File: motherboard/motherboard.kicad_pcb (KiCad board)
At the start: 2 copper layers, 85.3 x 56.5 mm, 87 parts, among them J1 power_conn, J2 serial_comm_conn, J3 Temp_connector, J5 24VDC_connector, P1 Raspberry_Pi_+_Conn, Q1 Q_NMOS_GSD, Q11 Q_NMOS_GSD, Q12 Q_NMOS_GSD, Q2 Q_NMOS_GSD, Q3 Q_NMOS_GSD, Q4 Q_NMOS_GSD, Q5 Q_NMOS_GSD, Q6 Q_NMOS_GSD, Q7 Q_NMOS_GSD, Q8 Q_NMOS_GSD, U1 LM324, U2 LM324, U4 MCP23017_ML, U5 74AUC2G04, U6 quad_and

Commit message: Do footprint assissiation
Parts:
- removed C1: C, Capacitor_SMD:C_0603_1608Metric
- removed C2, C3: 135pF, Capacitor_SMD:C_0603_1608Metric
- removed C4, C6, C8: 100nF, Capacitor_SMD:C_0603_1608Metric
- removed C5, C7, C9: 10pF, Capacitor_SMD:C_0603_1608Metric
- removed D1, D2: D, Diode_SMD:D_0603_1608Metric
- removed D10, D11, D12, D4, D5, D6, D7, D8, D9: LED, LED_SMD:LED_0603_1608Metric
- removed D3: d, Diode_SMD:D_0603_1608Metric
- removed J1: power_conn, TerminalBlock_Phoenix:TerminalBlock_Phoenix_MKDS-1,5-2-5.08_1x02_P5.08mm_Horizontal
- removed J2: serial_comm_conn, TerminalBlock_Phoenix:TerminalBlock_Phoenix_MKDS-1,5-3-5.08_1x03_P5.08mm_Horizontal
- removed J3: Temp_connector, TerminalBlock_Phoenix:TerminalBlock_Phoenix_MKDS-1,5-3-5.08_1x03_P5.08mm_Horizontal
- removed J5: 24VDC_connector, TerminalBlock_Phoenix:TerminalBlock_Phoenix_MKDS-1,5-8-5.08_1x08_P5.08mm_Horizontal
- removed P1: Raspberry_Pi_+_Conn, Connector_PinSocket_2.54mm:PinSocket_2x20_P2.54mm_Vertical
- removed Q1, Q11, Q12, Q2, Q3, Q4, Q5, Q6, Q7, Q8: Q_NMOS_GSD, Package_TO_SOT_SMD:SOT-23
- removed R1, R2: 100, Resistor_SMD:R_0603_1608Metric_Pad1.05x0.95mm_HandSolder
- removed R10, R12, R14, R16, R43, R45, R6, R8: 5, Resistor_SMD:R_0603_1608Metric_Pad1.05x0.95mm_HandSolder
- removed R11, R13, R15, R27, R28, R42, R44, R5, R7, R9: 100k, Resistor_SMD:R_0603_1608Metric_Pad1.05x0.95mm_HandSolder
- removed R17, R18, R19, R21, R32, R33, R34, R36: 4k7, Resistor_SMD:R_0603_1608Metric_Pad1.05x0.95mm_HandSolder
- removed R20, R22, R31, R35, R37, R38, R39, R40, R41: 240, Resistor_SMD:R_0603_1608Metric_Pad1.05x0.95mm_HandSolder
- removed R23, R24: 10k, Resistor_SMD:R_0603_1608Metric_Pad1.05x0.95mm_HandSolder
- removed R25, R26: 1k, Resistor_SMD:R_0603_1608Metric_Pad1.05x0.95mm_HandSolder
- removed R29: 3k3, Resistor_SMD:R_0603_1608Metric_Pad1.05x0.95mm_HandSolder
- removed R3: 4.7k, Resistor_SMD:R_0603_1608Metric_Pad1.05x0.95mm_HandSolder
- removed R30: 5k6, Resistor_SMD:R_0603_1608Metric_Pad1.05x0.95mm_HandSolder
- removed R4: 230, Resistor_SMD:R_0603_1608Metric_Pad1.05x0.95mm_HandSolder
- removed RV1: 10k, Potentiometer_SMD:Potentiometer_Vishay_TS53YL_Vertical
- removed U1, U2: LM324, Package_SO:TSSOP-14-1EP_4.4x5mm_P0.65mm
- removed U4: MCP23017_ML, Package_DFN_QFN:QFN-28-1EP_6x6mm_P0.65mm_EP4.25x4.25mm
- removed U5: 74AUC2G04, Package_TO_SOT_SMD:SOT-23-6
- removed U6: quad_and, Package_SO:SOIC-14_3.9x8.7mm_P1.27mm
- added C101: 1u, Capacitor_SMD:CP_Elec_4x5.4, F.Cu at (89.6, 43.2)
- added C102: 1u, Capacitor_SMD:CP_Elec_4x5.4, F.Cu at (74.1, 43.2)
- added C103: 1u, Capacitor_SMD:CP_Elec_4x5.4, F.Cu at (81.8, 43.2)
- added C104: 10n, Capacitor_SMD:C_0603_1608Metric_Pad1.05x0.95mm_HandSolder, F.Cu at (65.2, 94.4)
- added C105: 10n, Capacitor_SMD:C_0603_1608Metric_Pad1.05x0.95mm_HandSolder, F.Cu at (95.7, 41.5)
- added C106: 10n, Capacitor_SMD:C_0603_1608Metric_Pad1.05x0.95mm_HandSolder, F.Cu at (72.4, 47.4)
- added C107: 100p, Capacitor_SMD:C_0603_1608Metric_Pad1.05x0.95mm_HandSolder, F.Cu at (76.8, 47.4)
- added C108: 100p, Capacitor_SMD:C_0603_1608Metric_Pad1.05x0.95mm_HandSolder, F.Cu at (72.4, 49.9)
- added C109: 100p, Capacitor_SMD:C_0603_1608Metric_Pad1.05x0.95mm_HandSolder, F.Cu at (76.8, 49.9)
- added C1601: 100nF, Capacitor_SMD:C_0603_1608Metric_Pad1.05x0.95mm_HandSolder, F.Cu at (201.2, 94.5)
- added C1602: 10pF, Capacitor_SMD:C_0603_1608Metric_Pad1.05x0.95mm_HandSolder, F.Cu at (205.9, 91.1)
- added C1701: 100nF, Capacitor_SMD:C_0603_1608Metric_Pad1.05x0.95mm_HandSolder, F.Cu at (174.8, 120.1)
- added C1702: 10pF, Capacitor_SMD:C_0603_1608Metric_Pad1.05x0.95mm_HandSolder, F.Cu at (161.7, 130.3)
- added C201: 100u, Capacitor_SMD:CP_Elec_6.3x5.4_Nichicon, F.Cu at (224.7, 68.4)
- added C202: 10n, Capacitor_SMD:C_0603_1608Metric_Pad1.05x0.95mm_HandSolder, F.Cu at (212.1, 77.9)
- added C203: 68u, Capacitor_SMD:CP_Elec_6.3x5.8, F.Cu at (210.8, 72.6)
- added C204: 100n, Capacitor_SMD:C_0603_1608Metric_Pad1.05x0.95mm_HandSolder, F.Cu at (207.8, 77.9)
- added C2104: 330n, Capacitor_SMD:C_0603_1608Metric_Pad1.05x0.95mm_HandSolder, F.Cu at (142.1, 124.8)
- added C2105: 0.1u, Capacitor_SMD:C_0603_1608Metric_Pad1.05x0.95mm_HandSolder, F.Cu at (137.8, 127.3)
- added C2106: 100n, Capacitor_SMD:C_0603_1608Metric_Pad1.05x0.95mm_HandSolder, F.Cu at (137.0, 130.1)
- added C2107: 1u, Capacitor_SMD:CP_Elec_4x5.4, F.Cu at (119.6, 135.9)
- added C2201: 100n, Capacitor_SMD:C_0603_1608Metric_Pad1.05x0.95mm_HandSolder, F.Cu at (103.7, 121.9)
- added C301: 0.1u, Capacitor_SMD:C_0603_1608Metric_Pad1.05x0.95mm_HandSolder, F.Cu at (166.2, 110.8)
- added C302: 0.1u, Capacitor_SMD:C_0603_1608Metric_Pad1.05x0.95mm_HandSolder, F.Cu at (166.2, 113.3)
- added C303: 10u, Capacitor_SMD:CP_Elec_5x5.4, F.Cu at (159.6, 103.5)
- added C304: 10u, Capacitor_SMD:CP_Elec_5x5.4, F.Cu at (159.6, 110.3)
- added C401: 2u2, Capacitor_SMD:C_0603_1608Metric_Pad1.05x0.95mm_HandSolder, F.Cu at (231.0, 46.5)
- added C402: 10u, Capacitor_SMD:CP_Elec_5x5.4, F.Cu at (211.8, 53.9)
- added C403: 2u2, Capacitor_SMD:C_0603_1608Metric_Pad1.05x0.95mm_HandSolder, F.Cu at (235.3, 41.5)
- added C404: 2u2, Capacitor_SMD:C_0603_1608Metric_Pad1.05x0.95mm_HandSolder, F.Cu at (235.3, 44.0)
- added C405: 2u2, Capacitor_SMD:C_0603_1608Metric_Pad1.05x0.95mm_HandSolder, F.Cu at (231.0, 49.1)
- added C406: 2u2, Capacitor_SMD:C_0603_1608Metric_Pad1.05x0.95mm_HandSolder, F.Cu at (222.8, 56.6)
- added C501: 2u2, Capacitor_SMD:C_0603_1608Metric_Pad1.05x0.95mm_HandSolder, F.Cu at (195.9, 75.6)
- added C502: 10u, Capacitor_SMD:CP_Elec_5x5.4, F.Cu at (180.4, 77.5)
- added C503: 2u2, Capacitor_SMD:C_0603_1608Metric_Pad1.05x0.95mm_HandSolder, F.Cu at (191.4, 81.7)
- added C504: 2u2, Capacitor_SMD:C_0603_1608Metric_Pad1.05x0.95mm_HandSolder, F.Cu at (200.2, 70.6)
- added C505: 2u2, Capacitor_SMD:C_0603_1608Metric_Pad1.05x0.95mm_HandSolder, F.Cu at (178.2, 82.2)
- added C506: 2u2, Capacitor_SMD:C_0603_1608Metric_Pad1.05x0.95mm_HandSolder, F.Cu at (187.1, 81.7)
- added C601: 100pF, Capacitor_SMD:C_0603_1608Metric_Pad1.05x0.95mm_HandSolder, F.Cu at (227.2, 88.7)
- added C602: 100pF, Capacitor_SMD:C_0603_1608Metric_Pad1.05x0.95mm_HandSolder, F.Cu at (231.7, 86.6)
- added C603: 100nF, Capacitor_SMD:C_0603_1608Metric_Pad1.05x0.95mm_HandSolder, F.Cu at (231.7, 84.1)
- added C604: 10pF, Capacitor_SMD:C_0603_1608Metric_Pad1.05x0.95mm_HandSolder, F.Cu at (214.3, 92.4)
- added C701: 220n, Capacitor_SMD:C_0603_1608Metric_Pad1.05x0.95mm_HandSolder, F.Cu at (97.7, 132.2)
- added D1601: LED, LED_SMD:LED_0603_1608Metric, F.Cu at (197.0, 97.0)
- added D1602: LED, LED_SMD:LED_0603_1608Metric, F.Cu at (201.0, 97.0)
- added D1603: LED, LED_SMD:LED_0603_1608Metric, F.Cu at (205.4, 93.7)
- added D1604: LED, LED_SMD:LED_0603_1608Metric, F.Cu at (205.1, 97.0)
- added D1701: LED, LED_SMD:LED_0603_1608Metric, F.Cu at (165.9, 128.6)
- added D1702: LED, LED_SMD:LED_0603_1608Metric, F.Cu at (169.9, 128.6)
- added D1703: LED, LED_SMD:LED_0603_1608Metric, F.Cu at (174.3, 125.2)
- added D1704: LED, LED_SMD:LED_0603_1608Metric, F.Cu at (174.0, 128.6)
- added D1801: LED, LED_SMD:LED_0603_1608Metric, F.Cu at (78.8, 137.3)
- added D2001: D, Diode_SMD:D_0603_1608Metric, F.Cu at (173.3, 91.2)
- added D2002: D, Diode_SMD:D_0603_1608Metric, F.Cu at (177.7, 88.6)
- added D201: 1N5817, Diode_THT:D_DO-41_SOD81_P10.16mm_Horizontal, F.Cu at (207.5, 66.4)
- added D2201: 1N457, Diode_THT:D_DO-41_SOD81_P10.16mm_Horizontal, F.Cu at (65.0, 102.2)
- added D2202: 1N457, Diode_THT:D_DO-41_SOD81_P10.16mm_Horizontal, F.Cu at (65.0, 106.4)
- added D2203: D, Diode_SMD:D_SMA-SMB_Universal_Handsoldering, F.Cu at (68.5, 115.6)
- added D2204: D, Diode_SMD:D_SMA-SMB_Universal_Handsoldering, F.Cu at (96.4, 102.8)
- added D2205: 1N457, Diode_THT:D_DO-41_SOD81_P10.16mm_Horizontal, F.Cu at (78.9, 102.2)
- added D2206: 1N457, Diode_THT:D_DO-41_SOD81_P10.16mm_Horizontal, F.Cu at (65.0, 110.7)
- added D2207: D, Diode_SMD:D_SMA-SMB_Universal_Handsoldering, F.Cu at (79.5, 115.6)
- added D2208: D, Diode_SMD:D_SMA-SMB_Universal_Handsoldering, F.Cu at (82.5, 107.1)
- added D2301: D, Diode_SMD:D_SMA-SMB_Universal_Handsoldering, F.Cu at (143.1, 108.4)
- added D2302: D, Diode_SMD:D_SMA-SMB_Universal_Handsoldering, F.Cu at (132.1, 113.9)
- added D2303: D, Diode_SMD:D_SMA-SMB_Universal_Handsoldering, F.Cu at (143.1, 102.8)
- added D2304: D, Diode_SMD:D_SMA-SMB_Universal_Handsoldering, F.Cu at (132.1, 108.4)
- added D2305: D, Diode_SMD:D_SMA-SMB_Universal_Handsoldering, F.Cu at (121.2, 113.9)
- added D2306: D, Diode_SMD:D_SMA-SMB_Universal_Handsoldering, F.Cu at (132.1, 102.8)
- added D2307: D, Diode_SMD:D_SMA-SMB_Universal_Handsoldering, F.Cu at (121.2, 108.4)
- added D2308: D, Diode_SMD:D_SMA-SMB_Universal_Handsoldering, F.Cu at (121.2, 102.8)
- added D2401: D, Diode_SMD:D_SMA-SMB_Universal_Handsoldering, F.Cu at (172.4, 48.6)
- added D2402: D, Diode_SMD:D_SMA-SMB_Universal_Handsoldering, F.Cu at (172.4, 43.0)
- added D2403: D, Diode_SMD:D_SMA-SMB_Universal_Handsoldering, F.Cu at (194.3, 48.6)
- added D2404: D, Diode_SMD:D_SMA-SMB_Universal_Handsoldering, F.Cu at (183.3, 43.0)
- added D2405: D, Diode_SMD:D_SMA-SMB_Universal_Handsoldering, F.Cu at (172.4, 54.1)
- added D2406: D, Diode_SMD:D_SMA-SMB_Universal_Handsoldering, F.Cu at (183.3, 48.6)
- added D2407: D, Diode_SMD:D_SMA-SMB_Universal_Handsoldering, F.Cu at (194.3, 43.0)
- added D2408: D, Diode_SMD:D_SMA-SMB_Universal_Handsoldering, F.Cu at (183.3, 54.1)
- added D701: d, Diode_SMD:D_SMA-SMB_Universal_Handsoldering, F.Cu at (90.0, 133.7)
- added F2401: 160mA, Fuse:Fuse_1206_3216Metric_Pad1.42x1.75mm_HandSolder, F.Cu at (169.9, 58.6)
- added G***: LOGO, graphic:bryggans_logo, F.Cu at (121.0, 70.0)
- added IC2101: ADS124S08IPBSR, Package_QFP:LQFP-32_5x5mm_P0.5mm, F.Cu at (120.4, 128.3)
- added JP1801: Jumper_3_Bridged12, Connector_PinHeader_2.54mm:PinHeader_1x03_P2.54mm_Vertical, F.Cu at (70.0, 133.3)
- added JP1802: Jumper_3_Bridged12, Connector_PinHeader_2.54mm:PinHeader_1x03_P2.54mm_Vertical, F.Cu at (65.4, 133.3)
- added JP301: Jumper, Connector_PinHeader_2.54mm:PinHeader_1x02_P2.54mm_Vertical, F.Cu at (173.8, 102.4)
- added JP302: Jumper, Connector_PinHeader_2.54mm:PinHeader_1x02_P2.54mm_Vertical, F.Cu at (178.4, 102.4)
- added JP601: Jumper, Connector_PinHeader_2.54mm:PinHeader_1x02_P2.54mm_Vertical, F.Cu at (222.7, 85.2)
- added L201: 220n, Inductor_SMD:L_Wuerth_HCI-5040, F.Cu at (228.3, 75.8)
- added P101: Raspberry_Pi_+_Conn, Connector_PinSocket_2.54mm:PinSocket_2x20_P2.54mm_Vertical, F.Cu at (67.9, 42.6)
- added Q1001: Q_NMOS_GSD, Package_TO_SOT_SMD:SOT-23, F.Cu at (183.2, 122.2)
- added Q1101: Q_NMOS_GSD, Package_TO_SOT_SMD:SOT-23, F.Cu at (149.9, 137.0)
- added Q1201: Q_NMOS_GSD, Package_TO_SOT_SMD:SOT-23, F.Cu at (162.4, 137.0)
- added Q1301: Q_NMOS_GSD, Package_TO_SOT_SMD:SOT-23, F.Cu at (188.4, 113.8)
- added Q1401: Q_NMOS_GSD, Package_TO_SOT_SMD:SOT-23, F.Cu at (214.3, 100.9)
- added Q1501: Q_NMOS_GSD, Package_TO_SOT_SMD:SOT-23, F.Cu at (174.9, 137.0)
- added Q2101: Q_NMOS_GSD, Package_TO_SOT_SMD:SOT-23, F.Cu at (132.6, 131.1)
- added Q2501: Q_NMOS_GSD, Package_TO_SOT_SMD:SOT-23, F.Cu at (195.8, 122.2)
- added Q501: Q_NMOS_GSD, Package_TO_SOT_SMD:SOT-23, F.Cu at (187.2, 75.7)
- added Q502: Q_NMOS_GSD, Package_TO_SOT_SMD:SOT-23, F.Cu at (186.7, 71.1)
- added Q503: Q_NMOS_GSD, Package_TO_SOT_SMD:SOT-23, F.Cu at (191.1, 66.6)
- added Q504: Q_NMOS_GSD, Package_TO_SOT_SMD:SOT-23, F.Cu at (186.7, 66.6)
- added Q601: Q_NMOS_GSD, Package_TO_SOT_SMD:SOT-23, F.Cu at (222.6, 92.3)
- added Q602: Q_NMOS_GSD, Package_TO_SOT_SMD:SOT-23, F.Cu at (227.2, 85.1)
- added Q801: Q_NMOS_GSD, Package_TO_SOT_SMD:SOT-23, F.Cu at (201.0, 105.5)
- added Q901: Q_NMOS_GSD, Package_TO_SOT_SMD:SOT-23, F.Cu at (188.4, 105.5)
- added R1001: 100k, Resistor_SMD:R_0603_1608Metric_Pad1.05x0.95mm_HandSolder, F.Cu at (187.7, 123.7)
- added R1002: 5.6, Resistor_SMD:R_0603_1608Metric_Pad1.05x0.95mm_HandSolder, F.Cu at (187.7, 121.2)
- added R1101: 100k, Resistor_SMD:R_0603_1608Metric_Pad1.05x0.95mm_HandSolder, F.Cu at (154.3, 138.5)
- added R1102: 5.6, Resistor_SMD:R_0603_1608Metric_Pad1.05x0.95mm_HandSolder, F.Cu at (154.3, 136.0)
- added R1201: 100k, Resistor_SMD:R_0603_1608Metric_Pad1.05x0.95mm_HandSolder, F.Cu at (166.8, 138.5)
- added R1202: 5.6, Resistor_SMD:R_0603_1608Metric_Pad1.05x0.95mm_HandSolder, F.Cu at (166.8, 136.0)
- added R1301: 100k, Resistor_SMD:R_0603_1608Metric_Pad1.05x0.95mm_HandSolder, F.Cu at (192.8, 115.3)
- added R1302: 5.6, Resistor_SMD:R_0603_1608Metric_Pad1.05x0.95mm_HandSolder, F.Cu at (192.8, 112.8)
- added R1401: 100k, Resistor_SMD:R_0603_1608Metric_Pad1.05x0.95mm_HandSolder, F.Cu at (218.8, 102.4)
- added R1402: 5.6, Resistor_SMD:R_0603_1608Metric_Pad1.05x0.95mm_HandSolder, F.Cu at (218.8, 99.9)
- added R1501: 100k, Resistor_SMD:R_0603_1608Metric_Pad1.05x0.95mm_HandSolder, F.Cu at (179.3, 138.5)
- added R1502: 5.6, Resistor_SMD:R_0603_1608Metric_Pad1.05x0.95mm_HandSolder, F.Cu at (179.3, 136.0)
- added R1601: 4k7, Resistor_SMD:R_0603_1608Metric_Pad1.05x0.95mm_HandSolder, F.Cu at (205.9, 88.6)
- added R1602: 220, Resistor_SMD:R_0603_1608Metric_Pad1.05x0.95mm_HandSolder, F.Cu at (192.8, 98.8)
- added R1603: 4k7, Resistor_SMD:R_0603_1608Metric_Pad1.05x0.95mm_HandSolder, F.Cu at (196.8, 94.5)
- added R1604: 220, Resistor_SMD:R_0805_2012Metric_Pad1.15x1.40mm_HandSolder, F.Cu at (197.1, 91.8)
- added R1605: 4k7, Resistor_SMD:R_0603_1608Metric_Pad1.05x0.95mm_HandSolder, F.Cu at (201.6, 88.6)
- added R1606: 220, Resistor_SMD:R_0805_2012Metric_Pad1.15x1.40mm_HandSolder, F.Cu at (197.1, 88.8)
- added R1607: 4k7, Resistor_SMD:R_0603_1608Metric_Pad1.05x0.95mm_HandSolder, F.Cu at (188.4, 98.8)
- added R1608: 220, Resistor_SMD:R_0603_1608Metric_Pad1.05x0.95mm_HandSolder, F.Cu at (201.6, 91.1)
- added R1701: 4k7, Resistor_SMD:R_0603_1608Metric_Pad1.05x0.95mm_HandSolder, F.Cu at (157.3, 130.3)
- added R1702: 220, Resistor_SMD:R_0603_1608Metric_Pad1.05x0.95mm_HandSolder, F.Cu at (170.5, 120.1)
- added R1703: 4k7, Resistor_SMD:R_0603_1608Metric_Pad1.05x0.95mm_HandSolder, F.Cu at (165.8, 126.0)
- added R1704: 220, Resistor_SMD:R_0805_2012Metric_Pad1.15x1.40mm_HandSolder, F.Cu at (165.9, 120.3)
- added R1705: 4k7, Resistor_SMD:R_0603_1608Metric_Pad1.05x0.95mm_HandSolder, F.Cu at (170.5, 122.6)
- added R1706: 220, Resistor_SMD:R_0805_2012Metric_Pad1.15x1.40mm_HandSolder, F.Cu at (165.9, 123.3)
- added R1707: 4k7, Resistor_SMD:R_0603_1608Metric_Pad1.05x0.95mm_HandSolder, F.Cu at (170.1, 126.0)
- added R1708: 220, Resistor_SMD:R_0603_1608Metric_Pad1.05x0.95mm_HandSolder, F.Cu at (174.8, 122.6)
- added R1801: 100k, Resistor_SMD:R_0603_1608Metric_Pad1.05x0.95mm_HandSolder, F.Cu at (79.3, 132.2)
- added R1802: 100k, Resistor_SMD:R_0603_1608Metric_Pad1.05x0.95mm_HandSolder, F.Cu at (74.5, 135.2)
- added R1803: 3k3, Resistor_SMD:R_0603_1608Metric_Pad1.05x0.95mm_HandSolder, F.Cu at (79.3, 134.7)
- added R1804: 5k6, Resistor_SMD:R_0603_1608Metric_Pad1.05x0.95mm_HandSolder, F.Cu at (74.5, 137.7)
- added R1805: 220, Resistor_SMD:R_0805_2012Metric_Pad1.15x1.40mm_HandSolder, F.Cu at (74.8, 132.4)
- added R2001: 100, Resistor_SMD:R_0603_1608Metric_Pad1.05x0.95mm_HandSolder, F.Cu at (169.1, 91.1)
- added R2002: 100, Resistor_SMD:R_0603_1608Metric_Pad1.05x0.95mm_HandSolder, F.Cu at (173.4, 88.6)
- added R2003: 4.7k, Resistor_SMD:R_0603_1608Metric_Pad1.05x0.95mm_HandSolder, F.Cu at (169.1, 88.6)
- added R2101: R, Resistor_SMD:R_0603_1608Metric_Pad1.05x0.95mm_HandSolder, F.Cu at (137.0, 132.6)
- added R2102: 47R, Resistor_SMD:R_0603_1608Metric_Pad1.05x0.95mm_HandSolder, F.Cu at (142.1, 127.3)
- added R2103: R, Resistor_SMD:R_0603_1608Metric_Pad1.05x0.95mm_HandSolder, F.Cu at (134.3, 137.1)
- added R2104: 47R, Resistor_SMD:R_0603_1608Metric_Pad1.05x0.95mm_HandSolder, F.Cu at (141.3, 129.8)
- added R2105: 47R, Resistor_SMD:R_0603_1608Metric_Pad1.05x0.95mm_HandSolder, F.Cu at (141.3, 132.3)
- added R2106: 47R, Resistor_SMD:R_0603_1608Metric_Pad1.05x0.95mm_HandSolder, F.Cu at (138.7, 135.1)
- added R2107: 100k, Resistor_SMD:R_0603_1608Metric_Pad1.05x0.95mm_HandSolder, F.Cu at (125.6, 135.3)
- added R2108: 47R, Resistor_SMD:R_0603_1608Metric_Pad1.05x0.95mm_HandSolder, F.Cu at (125.6, 137.8)
- added R2109: 47R, Resistor_SMD:R_0603_1608Metric_Pad1.05x0.95mm_HandSolder, F.Cu at (130.0, 137.1)
- added R2110: 1k, Resistor_SMD:R_0603_1608Metric_Pad1.05x0.95mm_HandSolder, F.Cu at (137.8, 124.8)
- added R2111: 47R, Resistor_SMD:R_0603_1608Metric_Pad1.05x0.95mm_HandSolder, F.Cu at (132.5, 134.6)
- added R2201: 75R, Resistor_SMD:R_0603_1608Metric_Pad1.05x0.95mm_HandSolder, F.Cu at (79.2, 111.1)
- added R2202: 75R, Resistor_SMD:R_0603_1608Metric_Pad1.05x0.95mm_HandSolder, F.Cu at (107.3, 110.3)
- added R2203: 750R, Resistor_SMD:R_0603_1608Metric_Pad1.05x0.95mm_HandSolder, F.Cu at (69.6, 126.1)
- added R2204: 750R, Resistor_SMD:R_0603_1608Metric_Pad1.05x0.95mm_HandSolder, F.Cu at (74.0, 126.1)
- added R2205: 20k, Resistor_SMD:R_0603_1608Metric_Pad1.05x0.95mm_HandSolder, F.Cu at (87.2, 117.1)
- added R2206: 28k, Resistor_SMD:R_0603_1608Metric_Pad1.05x0.95mm_HandSolder, F.Cu at (78.3, 126.1)
- added R2207: 20k, Resistor_SMD:R_0603_1608Metric_Pad1.05x0.95mm_HandSolder, F.Cu at (65.2, 126.1)
- added R2208: 20k, Resistor_SMD:R_0603_1608Metric_Pad1.05x0.95mm_HandSolder, F.Cu at (98.6, 106.9)
- added R2209: 28k, Resistor_SMD:R_0603_1608Metric_Pad1.05x0.95mm_HandSolder, F.Cu at (95.8, 117.1)
- added R2210: 20k, Resistor_SMD:R_0603_1608Metric_Pad1.05x0.95mm_HandSolder, F.Cu at (90.6, 122.1)
- added R2211: 100k, Resistor_SMD:R_0603_1608Metric_Pad1.05x0.95mm_HandSolder, F.Cu at (90.6, 119.6)
- added R2212: 100k, Resistor_SMD:R_0603_1608Metric_Pad1.05x0.95mm_HandSolder, F.Cu at (91.5, 117.1)
- added R2213: 1k, Resistor_SMD:R_0603_1608Metric_Pad1.05x0.95mm_HandSolder, F.Cu at (82.7, 126.1)
- added R2214: 1k, Resistor_SMD:R_0603_1608Metric_Pad1.05x0.95mm_HandSolder, F.Cu at (98.6, 109.4)
- added R2215: 1k, Resistor_SMD:R_0603_1608Metric_Pad1.05x0.95mm_HandSolder, F.Cu at (102.9, 107.8)
- added R2216: 1k, Resistor_SMD:R_0603_1608Metric_Pad1.05x0.95mm_HandSolder, F.Cu at (83.5, 111.1)
- added R2217: 75R, Resistor_SMD:R_0603_1608Metric_Pad1.05x0.95mm_HandSolder, F.Cu at (99.3, 119.6)
- added R2218: 75R, Resistor_SMD:R_0603_1608Metric_Pad1.05x0.95mm_HandSolder, F.Cu at (95.7, 124.6)
- added R2219: 750R, Resistor_SMD:R_0603_1608Metric_Pad1.05x0.95mm_HandSolder, F.Cu at (107.3, 112.8)
- added R2220: 750R, Resistor_SMD:R_0603_1608Metric_Pad1.05x0.95mm_HandSolder, F.Cu at (99.3, 122.1)
- added R2221: 20k, Resistor_SMD:R_0603_1608Metric_Pad1.05x0.95mm_HandSolder, F.Cu at (87.0, 126.1)
- added R2222: 28k, Resistor_SMD:R_0603_1608Metric_Pad1.05x0.95mm_HandSolder, F.Cu at (98.6, 111.9)
- added R2223: 20k, Resistor_SMD:R_0603_1608Metric_Pad1.05x0.95mm_HandSolder, F.Cu at (91.3, 124.6)
- added R2224: 20k, Resistor_SMD:R_0603_1608Metric_Pad1.05x0.95mm_HandSolder, F.Cu at (100.2, 116.9)
- added R2225: 28k, Resistor_SMD:R_0603_1608Metric_Pad1.05x0.95mm_HandSolder, F.Cu at (102.9, 112.8)
- added R2226: 20k, Resistor_SMD:R_0603_1608Metric_Pad1.05x0.95mm_HandSolder, F.Cu at (95.0, 122.1)
- added R2227: 100k, Resistor_SMD:R_0603_1608Metric_Pad1.05x0.95mm_HandSolder, F.Cu at (95.0, 119.6)
- added R2228: 100k, Resistor_SMD:R_0603_1608Metric_Pad1.05x0.95mm_HandSolder, F.Cu at (107.3, 107.8)
- added R2229: 1k, Resistor_SMD:R_0603_1608Metric_Pad1.05x0.95mm_HandSolder, F.Cu at (102.9, 110.3)
- added R2230: 1k, Resistor_SMD:R_0603_1608Metric_Pad1.05x0.95mm_HandSolder, F.Cu at (98.6, 114.4)
- added R2231: 1k, Resistor_SMD:R_0603_1608Metric_Pad1.05x0.95mm_HandSolder, F.Cu at (104.5, 115.3)
- added R2232: 1k, Resistor_SMD:R_0603_1608Metric_Pad1.05x0.95mm_HandSolder, F.Cu at (103.7, 119.4)
- added R2233: 2k7, Resistor_SMD:R_0603_1608Metric_Pad1.05x0.95mm_HandSolder, F.Cu at (126.6, 118.0)
- added R2234: 2k7, Resistor_SMD:R_0603_1608Metric_Pad1.05x0.95mm_HandSolder, F.Cu at (130.9, 118.0)
- added R2235: 2k7, Resistor_SMD:R_0603_1608Metric_Pad1.05x0.95mm_HandSolder, F.Cu at (144.1, 112.4)
- added R2301: 10k, Resistor_SMD:R_0603_1608Metric_Pad1.05x0.95mm_HandSolder, F.Cu at (135.3, 118.0)
- added R2302: 2k7, Resistor_SMD:R_0603_1608Metric_Pad1.05x0.95mm_HandSolder, F.Cu at (139.8, 117.4)
- added R2303: 10k, Resistor_SMD:R_0603_1608Metric_Pad1.05x0.95mm_HandSolder, F.Cu at (139.8, 114.9)
- added R2304: 120R, Resistor_SMD:R_0805_2012Metric_Pad1.15x1.40mm_HandSolder, F.Cu at (191.2, 52.9)
- added R2305: 10k, Resistor_SMD:R_0603_1608Metric_Pad1.05x0.95mm_HandSolder, F.Cu at (139.8, 112.4)
- added R2306: 120R, Resistor_SMD:R_0805_2012Metric_Pad1.15x1.40mm_HandSolder, F.Cu at (184.8, 58.4)
- added R2307: 10k, Resistor_SMD:R_0603_1608Metric_Pad1.05x0.95mm_HandSolder, F.Cu at (117.9, 118.0)
- added R2308: 120R, Resistor_SMD:R_0805_2012Metric_Pad1.15x1.40mm_HandSolder, F.Cu at (175.2, 58.4)
- added R2309: 1k, Resistor_SMD:R_0603_1608Metric_Pad1.05x0.95mm_HandSolder, F.Cu at (144.1, 114.9)
- added R2310: 1k, Resistor_SMD:R_0603_1608Metric_Pad1.05x0.95mm_HandSolder, F.Cu at (122.2, 118.0)
- added R2311: 1k, Resistor_SMD:R_0603_1608Metric_Pad1.05x0.95mm_HandSolder, F.Cu at (148.5, 112.4)
- added R2312: 1k, Resistor_SMD:R_0603_1608Metric_Pad1.05x0.95mm_HandSolder, F.Cu at (144.1, 117.4)
- added R2401: 120R, Resistor_SMD:R_0805_2012Metric_Pad1.15x1.40mm_HandSolder, F.Cu at (180.0, 58.4)
- added R2405: 1k, Resistor_SMD:R_0603_1608Metric_Pad1.05x0.95mm_HandSolder, F.Cu at (200.1, 52.6)
- added R2406: 1k, Resistor_SMD:R_0603_1608Metric_Pad1.05x0.95mm_HandSolder, F.Cu at (195.8, 55.1)
- added R2407: 1k, Resistor_SMD:R_0603_1608Metric_Pad1.05x0.95mm_HandSolder, F.Cu at (201.9, 46.5)
- added R2408: 1k, Resistor_SMD:R_0603_1608Metric_Pad1.05x0.95mm_HandSolder, F.Cu at (189.3, 58.2)
- added R2409: 1k, Resistor_SMD:R_0603_1608Metric_Pad1.05x0.95mm_HandSolder, F.Cu at (191.0, 55.6)
- added R2410: 1k, Resistor_SMD:R_0603_1608Metric_Pad1.05x0.95mm_HandSolder, F.Cu at (195.8, 52.6)
- added R2411: 1k, Resistor_SMD:R_0603_1608Metric_Pad1.05x0.95mm_HandSolder, F.Cu at (201.9, 44.0)
- added R2412: 1k, Resistor_SMD:R_0603_1608Metric_Pad1.05x0.95mm_HandSolder, F.Cu at (201.9, 41.5)
- added R2501: 100k, Resistor_SMD:R_0603_1608Metric_Pad1.05x0.95mm_HandSolder, F.Cu at (200.2, 123.7)
- added R2502: 5.6, Resistor_SMD:R_0603_1608Metric_Pad1.05x0.95mm_HandSolder, F.Cu at (200.2, 121.2)
- added R301: 10k, Resistor_SMD:R_0603_1608Metric_Pad1.05x0.95mm_HandSolder, F.Cu at (177.9, 108.5)
- added R302: 10k, Resistor_SMD:R_0603_1608Metric_Pad1.05x0.95mm_HandSolder, F.Cu at (173.6, 108.5)
- added R401: 22k, Resistor_SMD:R_0603_1608Metric_Pad1.05x0.95mm_HandSolder, F.Cu at (227.1, 51.6)
- added R402: 22k, Resistor_SMD:R_0603_1608Metric_Pad1.05x0.95mm_HandSolder, F.Cu at (226.6, 41.5)
- added R403: 22k, Resistor_SMD:R_0603_1608Metric_Pad1.05x0.95mm_HandSolder, F.Cu at (222.3, 41.5)
- added R404: 22k, Resistor_SMD:R_0603_1608Metric_Pad1.05x0.95mm_HandSolder, F.Cu at (217.9, 44.0)
- added R405: 1M, Resistor_SMD:R_0603_1608Metric_Pad1.05x0.95mm_HandSolder, F.Cu at (222.3, 44.0)
- added R406: 1M, Resistor_SMD:R_0603_1608Metric_Pad1.05x0.95mm_HandSolder, F.Cu at (217.9, 46.5)
- added R407: 1M, Resistor_SMD:R_0603_1608Metric_Pad1.05x0.95mm_HandSolder, F.Cu at (217.9, 49.1)
- added R408: 1M, Resistor_SMD:R_0603_1608Metric_Pad1.05x0.95mm_HandSolder, F.Cu at (218.4, 51.6)
- added R409: 3k9, Resistor_SMD:R_0603_1608Metric_Pad1.05x0.95mm_HandSolder, F.Cu at (222.3, 46.5)
- added R410: 3k9, Resistor_SMD:R_0603_1608Metric_Pad1.05x0.95mm_HandSolder, F.Cu at (222.8, 54.1)
- added R411: 3k9, Resistor_SMD:R_0603_1608Metric_Pad1.05x0.95mm_HandSolder, F.Cu at (226.6, 44.0)
- added R412: 3k9, Resistor_SMD:R_0603_1608Metric_Pad1.05x0.95mm_HandSolder, F.Cu at (222.3, 49.1)
- added R413: 6k8, Resistor_SMD:R_0603_1608Metric_Pad1.05x0.95mm_HandSolder, F.Cu at (218.4, 54.1)
- added R414: 6k8, Resistor_SMD:R_0603_1608Metric_Pad1.05x0.95mm_HandSolder, F.Cu at (222.8, 51.6)
- added R415: 6k8, Resistor_SMD:R_0603_1608Metric_Pad1.05x0.95mm_HandSolder, F.Cu at (226.6, 46.5)
- added R416: 6k8, Resistor_SMD:R_0603_1608Metric_Pad1.05x0.95mm_HandSolder, F.Cu at (231.0, 41.5)
- added R417: 1k2, Resistor_SMD:R_0603_1608Metric_Pad1.05x0.95mm_HandSolder, F.Cu at (218.4, 56.6)
- added R418: 1k2, Resistor_SMD:R_0603_1608Metric_Pad1.05x0.95mm_HandSolder, F.Cu at (226.6, 49.1)
- added R419: 1k2, Resistor_SMD:R_0603_1608Metric_Pad1.05x0.95mm_HandSolder, F.Cu at (231.0, 44.0)
- added R420: 1k2, Resistor_SMD:R_0603_1608Metric_Pad1.05x0.95mm_HandSolder, F.Cu at (217.9, 41.5)
- added R501: 22k, Resistor_SMD:R_0603_1608Metric_Pad1.05x0.95mm_HandSolder, F.Cu at (195.9, 73.1)
- added R502: 22k, Resistor_SMD:R_0603_1608Metric_Pad1.05x0.95mm_HandSolder, F.Cu at (182.5, 82.2)
- added R503: 22k, Resistor_SMD:R_0603_1608Metric_Pad1.05x0.95mm_HandSolder, F.Cu at (191.4, 79.2)
- added R504: 22k, Resistor_SMD:R_0603_1608Metric_Pad1.05x0.95mm_HandSolder, F.Cu at (195.5, 65.5)
- added R505: 1M, Resistor_SMD:R_0603_1608Metric_Pad1.05x0.95mm_HandSolder, F.Cu at (187.1, 79.2)
- added R506: 1M, Resistor_SMD:R_0603_1608Metric_Pad1.05x0.95mm_HandSolder, F.Cu at (199.8, 65.5)
- added R507: 1M, Resistor_SMD:R_0603_1608Metric_Pad1.05x0.95mm_HandSolder, F.Cu at (195.5, 68.0)
- added R508: 1M, Resistor_SMD:R_0603_1608Metric_Pad1.05x0.95mm_HandSolder, F.Cu at (191.1, 70.1)
- added R509: 180R, Resistor_SMD:R_2512_6332Metric_Pad1.52x3.35mm_HandSolder, F.Cu at (179.9, 66.7)
- added R510: 180R, Resistor_SMD:R_2512_6332Metric_Pad1.52x3.35mm_HandSolder, F.Cu at (171.4, 81.8)
- added R511: 180R, Resistor_SMD:R_2512_6332Metric_Pad1.52x3.35mm_HandSolder, F.Cu at (171.4, 76.9)
- added R512: 180R, Resistor_SMD:R_2512_6332Metric_Pad1.52x3.35mm_HandSolder, F.Cu at (179.9, 71.6)
- added R513: 100k, Resistor_SMD:R_0603_1608Metric_Pad1.05x0.95mm_HandSolder, F.Cu at (191.6, 75.1)
- added R514: 100k, Resistor_SMD:R_0603_1608Metric_Pad1.05x0.95mm_HandSolder, F.Cu at (199.8, 68.0)
- added R515: 100k, Resistor_SMD:R_0603_1608Metric_Pad1.05x0.95mm_HandSolder, F.Cu at (191.6, 72.6)
- added R516: 100k, Resistor_SMD:R_0603_1608Metric_Pad1.05x0.95mm_HandSolder, F.Cu at (195.9, 70.6)
- added R601: 10k, Resistor_SMD:R_0603_1608Metric_Pad1.05x0.95mm_HandSolder, F.Cu at (231.6, 89.1)
- added R602: 10k, Resistor_SMD:R_0603_1608Metric_Pad1.05x0.95mm_HandSolder, F.Cu at (231.3, 94.2)
- added R603: 1k, Resistor_SMD:R_0603_1608Metric_Pad1.05x0.95mm_HandSolder, F.Cu at (231.6, 91.7)
- added R604: 1k, Resistor_SMD:R_0603_1608Metric_Pad1.05x0.95mm_HandSolder, F.Cu at (227.0, 93.7)
- added R605: 10k, Resistor_SMD:R_0603_1608Metric_Pad1.05x0.95mm_HandSolder, F.Cu at (227.2, 91.2)
- added R701: 220, Resistor_SMD:R_0805_2012Metric_Pad1.15x1.40mm_HandSolder, F.Cu at (86.9, 138.0)
- added R801: 100k, Resistor_SMD:R_0603_1608Metric_Pad1.05x0.95mm_HandSolder, F.Cu at (205.4, 104.5)
- added R802: 5.6, Resistor_SMD:R_0603_1608Metric_Pad1.05x0.95mm_HandSolder, F.Cu at (205.4, 107.0)
- added R901: 100k, Resistor_SMD:R_0603_1608Metric_Pad1.05x0.95mm_HandSolder, F.Cu at (192.8, 107.0)
- added R902: 5.6, Resistor_SMD:R_0603_1608Metric_Pad1.05x0.95mm_HandSolder, F.Cu at (192.8, 104.5)
- added TP2101: TestPoint, TestPoint:TestPoint_Loop_D3.50mm_Drill1.4mm_Beaded, F.Cu at (127.7, 126.2)
- added TP2102: TestPoint, TestPoint:TestPoint_Loop_D3.50mm_Drill1.4mm_Beaded, F.Cu at (133.0, 126.2)
- added TP2103: TestPoint, TestPoint:TestPoint_Loop_D3.50mm_Drill1.4mm_Beaded, F.Cu at (127.7, 131.4)
- added U1601: LM324, Package_SO:SOIC-14_3.9x8.7mm_P1.27mm, F.Cu at (190.4, 92.5)
- added U1701: LM324, Package_SO:SOIC-14_3.9x8.7mm_P1.27mm, F.Cu at (159.3, 124.0)
- added U201: LM2674M-12, Package_SO:SOIC-8_3.9x4.9mm_P1.27mm, F.Cu at (220.3, 75.7)
- added U2201: LM324, Package_SO:SOIC-14_3.9x8.7mm_P1.27mm, F.Cu at (92.2, 110.7)
- added U2202: LM334M, Package_SO:SOIC-8_3.9x4.9mm_P1.27mm, F.Cu at (106.1, 103.3)
- added U2203: LM334M, Package_SO:SOIC-8_3.9x4.9mm_P1.27mm, F.Cu at (75.8, 121.6)
- added U2204: LM334M, Package_SO:SOIC-8_3.9x4.9mm_P1.27mm, F.Cu at (67.3, 121.6)
- added U2205: LM334M, Package_SO:SOIC-8_3.9x4.9mm_P1.27mm, F.Cu at (84.2, 121.6)
- added U301: MCP4728, Package_SO:MSOP-10_3x3mm_P0.5mm, F.Cu at (167.8, 102.4)
- added U302: MCP4728, Package_SO:MSOP-10_3x3mm_P0.5mm, F.Cu at (167.8, 107.2)
- added U401: LM324, Package_SO:SOIC-14_3.9x8.7mm_P1.27mm, F.Cu at (211.5, 45.4)
- added U501: LM324, Package_SO:SOIC-14_3.9x8.7mm_P1.27mm, F.Cu at (171.2, 69.4)
- added U601: MCP23017_ML, Package_DFN_QFN:QFN-28-1EP_6x6mm_P0.65mm_EP4.25x4.25mm, F.Cu at (216.2, 87.0)
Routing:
- net Net-(C2-Pad1): track 14.0 -> 0.00 mm
- net +5V: track 6.87 -> 0.00 mm
- net /SSR_interface/SSR1_GPIO_safe: track 5.40 -> 0.00 mm
- net Net-(C3-Pad1): track 5.06 -> 0.00 mm
- net /low_side_outputs/SSR1_driver/indicator: track 4.33 -> 0.00 mm
- net +3V3: track 3.90 -> 0.00 mm
- net /i2c_interface/sda: track 1.96 -> 0.00 mm
- net /i2c_interface/sck: track 1.83 -> 0.00 mm
- removed copper zone on B.Cu, net GND
- removed copper zone on F.Cu, net GND
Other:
- board outline removed

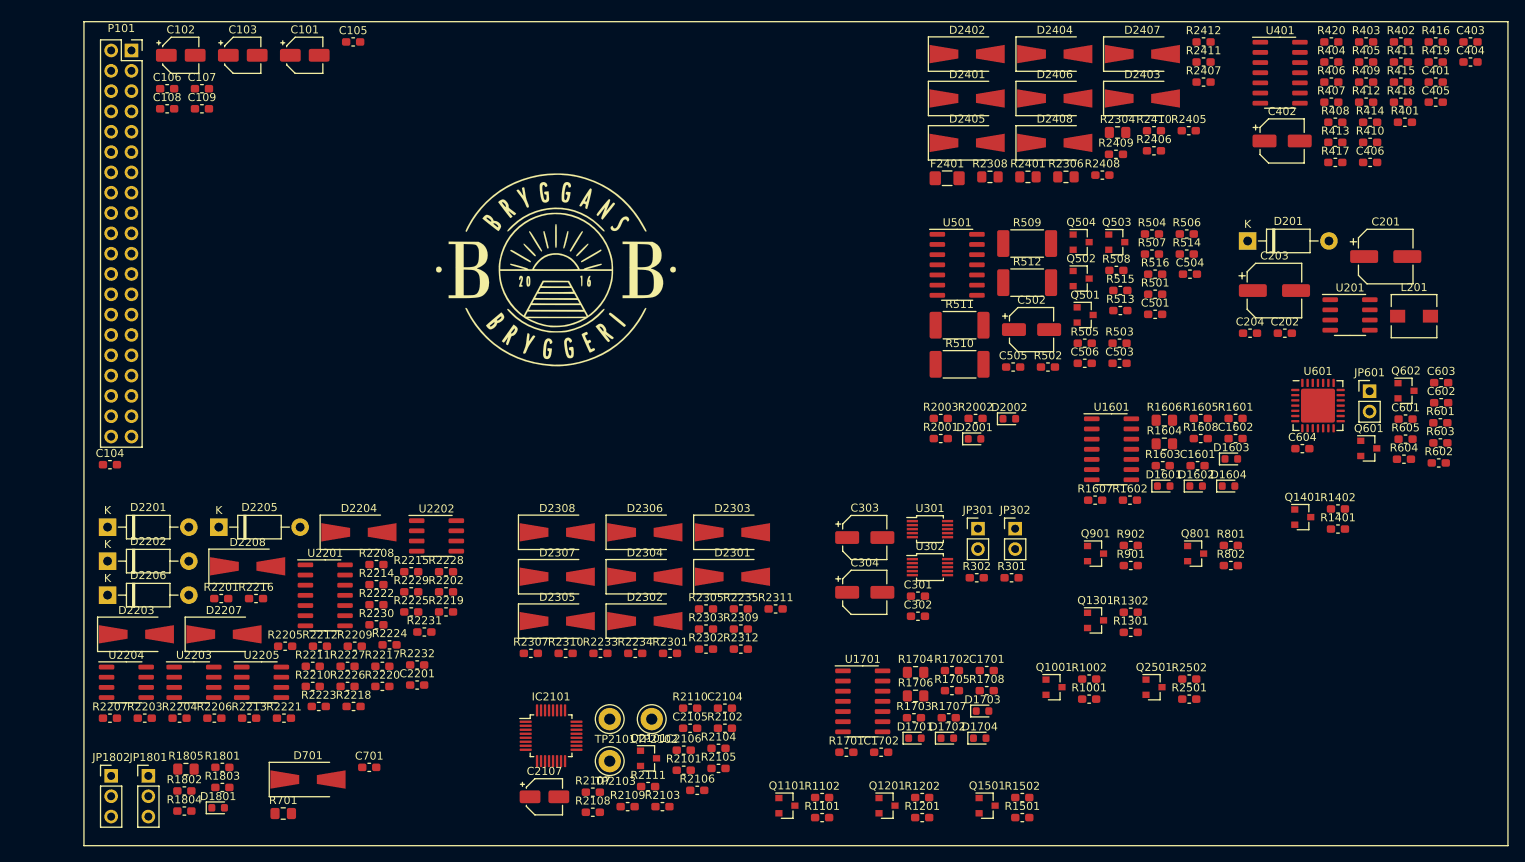
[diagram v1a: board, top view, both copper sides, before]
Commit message: Double diodes, removed v_ref buffer.
fixes #83
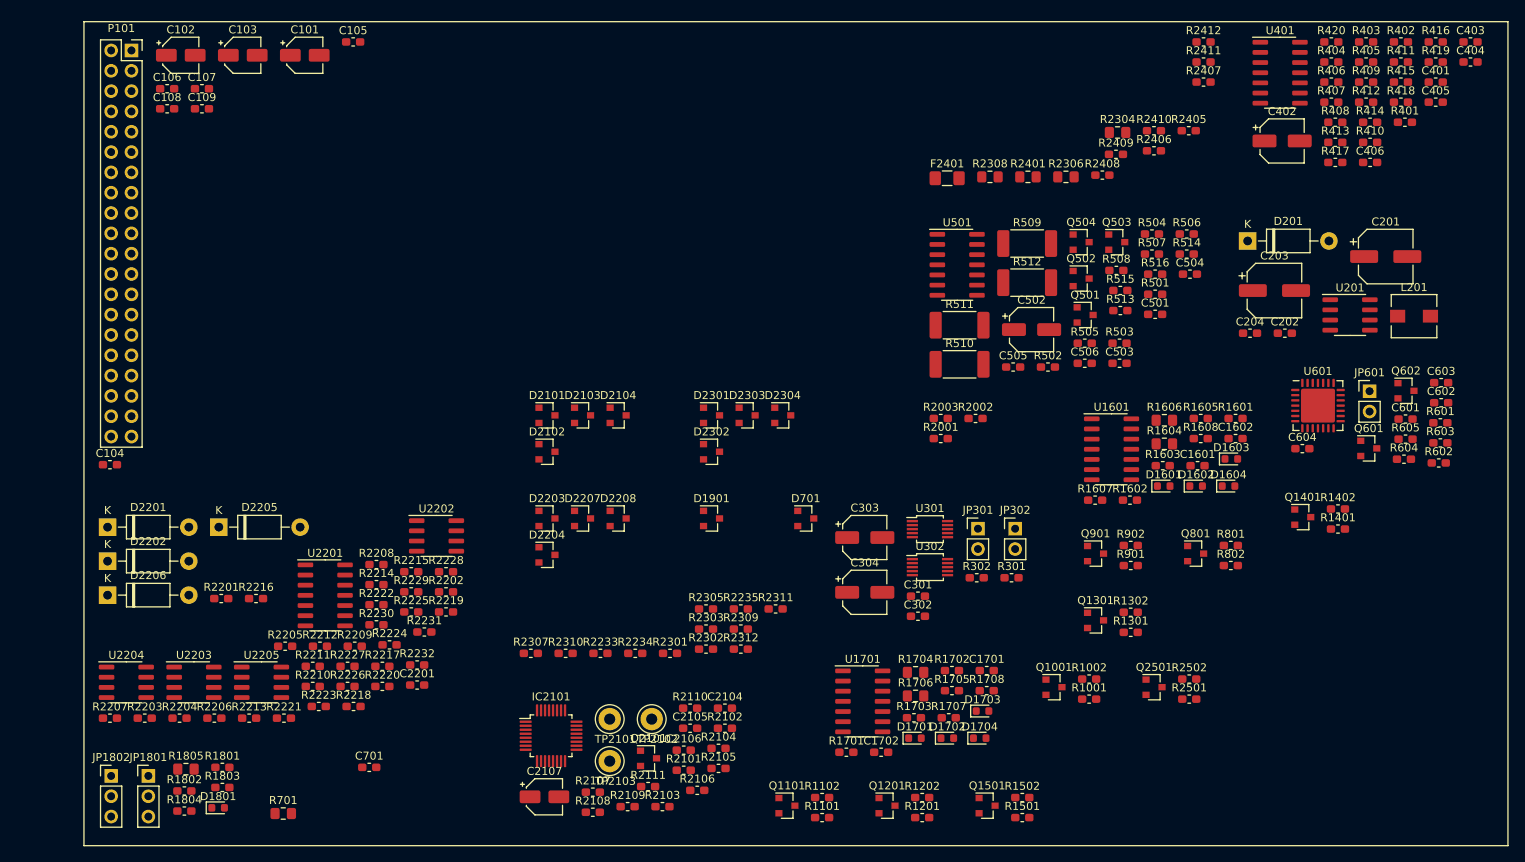
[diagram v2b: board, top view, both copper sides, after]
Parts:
- removed D2001, D2002: D, Diode_SMD:D_0603_1608Metric
- removed D2305, D2306, D2307, D2308, D2401, D2402, D2403, D2404, D2405, D2406, D2407, D2408: D, Diode_SMD:D_SMA-SMB_Universal_Handsoldering
- removed G***: LOGO, graphic:bryggans_logo
- added D1901: BAT54S, Package_TO_SOT_SMD:SOT-23, F.Cu at (140.4, 101.1)
- added D2101: BAT54S, Package_TO_SOT_SMD:SOT-23, F.Cu at (119.9, 88.2)
- added D2102: BAT54S, Package_TO_SOT_SMD:SOT-23, F.Cu at (119.9, 92.8)
- added D2103: BAT54S, Package_TO_SOT_SMD:SOT-23, F.Cu at (124.3, 88.2)
- added D2104: BAT54S, Package_TO_SOT_SMD:SOT-23, F.Cu at (128.8, 88.2)
- D2203, D2204, D2207, D2208, D2301, D2302, D2303, D2304: value D -> BAT54S; footprint Diode_SMD:D_SMA-SMB_Universal_Handsoldering -> Package_TO_SOT_SMD:SOT-23
- D701: value d -> BAT54S; footprint Diode_SMD:D_SMA-SMB_Universal_Handsoldering -> Package_TO_SOT_SMD:SOT-23
- moved D701 70.3 mm to (152.2, 101.1)
- moved D2203 53.3 mm to (119.9, 101.1)
- moved D2207 47.1 mm to (124.3, 101.1)
- moved D2208 46.7 mm to (128.8, 101.1)
- moved D2304 26.5 mm to (149.3, 88.2)
- moved D2204 23.7 mm to (119.9, 105.7)
- moved D2302 22.8 mm to (140.4, 92.8)
- moved D2301 20.3 mm to (140.4, 88.2)
- moved D2303 14.7 mm to (144.9, 88.2)
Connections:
- D2201 pad 2: (no net) -> Net-(D2201-Pad2)
- D2202 pad 2: (no net) -> Net-(D2202-Pad2)
- D2203 pad 1: /Analog inputs/Vref_buf -> GND
- D2203 pad 2: Net-(D2203-Pad2) -> /Analog inputs/Vref_buf
- D2204 pad 1: /Analog inputs/Vref_buf -> GND
- D2204 pad 2: Net-(D2204-Pad2) -> /Analog inputs/Vref_buf
- D2205 pad 2: (no net) -> Net-(D2205-Pad2)
- D2206 pad 2: (no net) -> Net-(D2206-Pad2)
- D2207 pad 1: /Analog inputs/Vref_buf -> GND
- D2207 pad 2: Net-(D2207-Pad2) -> /Analog inputs/Vref_buf
- D2208 pad 1: /Analog inputs/Vref_buf -> GND
- D2208 pad 2: Net-(D2208-Pad2) -> /Analog inputs/Vref_buf
- D2301 pad 1: /Analog inputs/Vref_buf -> GND
- D2301 pad 2: Net-(D2301-Pad2) -> /Analog inputs/20mA-1-4/Vref
- D2302 pad 1: Net-(D2301-Pad2) -> GND
- D2302 pad 2: GND -> /Analog inputs/20mA-1-4/Vref
- D2303 pad 1: /Analog inputs/Vref_buf -> GND
- D2303 pad 2: Net-(D2303-Pad2) -> /Analog inputs/20mA-1-4/Vref
- D2304 pad 1: Net-(D2303-Pad2) -> GND
- D2304 pad 2: GND -> /Analog inputs/20mA-1-4/Vref
- D701 pad 1: GND -> Net-(D701-Pad1)
- D701 pad 2: Net-(D701-Pad2) -> GND
- F2401 pad 1: (no net) -> /Analog inputs/20mA-1-4/A_in_high
- IC2101 pad 25: (no net) -> Net-(IC2101-Pad25)
- IC2101 pad 29: (no net) -> Net-(IC2101-Pad29)
- IC2101 pad 30: (no net) -> Net-(IC2101-Pad30)
- JP1801 pad 1: (no net) -> Net-(JP1801-Pad1)
- JP1802 pad 1: (no net) -> Net-(JP1802-Pad1)
- P101 pad 10: (no net) -> /VFD_comm/rxd_pi
- P101 pad 11: (no net) -> Net-(P101-Pad11)
- P101 pad 12: (no net) -> Net-(P101-Pad12)
- P101 pad 13: (no net) -> Net-(P101-Pad13)
- P101 pad 15: (no net) -> Net-(P101-Pad15)
- P101 pad 17: (no net) -> Net-(P101-Pad17)
- P101 pad 22: (no net) -> Net-(P101-Pad22)
- P101 pad 26: (no net) -> Net-(P101-Pad26)
- P101 pad 27: (no net) -> Net-(P101-Pad27)
- P101 pad 28: (no net) -> Net-(P101-Pad28)
- P101 pad 29: (no net) -> Net-(P101-Pad29)
- P101 pad 31: (no net) -> Net-(P101-Pad31)
- P101 pad 35: (no net) -> Net-(P101-Pad35)
- P101 pad 37: (no net) -> Net-(P101-Pad37)
- P101 pad 38: (no net) -> Net-(P101-Pad38)
- P101 pad 40: (no net) -> Net-(P101-Pad40)
- P101 pad 8: (no net) -> /VFD_comm/txd_pi
- Q1001 pad 3: (no net) -> /SSR_1_enclosure
- Q1101 pad 3: (no net) -> /extra_1_enclosure
- Q1201 pad 3: (no net) -> /extra_2_enclosure
- Q1301 pad 3: (no net) -> /relay_3_enclosure
- Q1401 pad 3: (no net) -> /relay_2_enclosure
- Q1501 pad 3: (no net) -> /relay_1_enclosure
- Q2501 pad 3: (no net) -> /Safety stop/drain
- Q501 pad 3: (no net) -> /DAC/B_out_20mA_high
- Q502 pad 3: (no net) -> /DAC/C_out_20mA_high
- Q503 pad 3: (no net) -> /DAC/D_out_20mA_high
- Q504 pad 3: (no net) -> /DAC/A_out_20mA_high
- Q801 pad 3: (no net) -> /SSR_2_enclosure
- Q901 pad 3: (no net) -> /relay_4_enclosure
- R2103 pad 2: (no net) -> /Analog inputs/Vref_inter
- R2201 pad 1: (no net) -> Net-(R2201-Pad1)
- R2202 pad 1: (no net) -> Net-(R2202-Pad1)
- R2207 pad 2: (no net) -> /Analog inputs/PT-100-1/A_tap
- R2209 pad 2: (no net) -> /Analog inputs/PT-100-1/C_pos
- R2210 pad 2: (no net) -> /Analog inputs/PT-100-1/C_tap
- R2213 pad 1: Net-(D2203-Pad2) -> Net-(D2101-Pad3)
- R2214 pad 1: Net-(D2204-Pad2) -> Net-(D2102-Pad3)
- R2215 pad 2: Net-(D2203-Pad2) -> Net-(D2101-Pad3)
- R2216 pad 2: Net-(D2204-Pad2) -> Net-(D2102-Pad3)
- R2217 pad 1: (no net) -> Net-(R2217-Pad1)
- R2218 pad 1: (no net) -> Net-(R2218-Pad1)
- R2222 pad 2: (no net) -> /Analog inputs/PT-100-1/B_pos
- R2223 pad 2: (no net) -> /Analog inputs/PT-100-1/B_tap
- R2225 pad 2: (no net) -> /Analog inputs/PT-100-1/D_pos
- R2226 pad 2: (no net) -> /Analog inputs/PT-100-1/D_tap
- R2229 pad 1: Net-(D2207-Pad2) -> Net-(D2103-Pad3)
- R2230 pad 1: Net-(D2208-Pad2) -> Net-(D2104-Pad3)
- R2231 pad 2: Net-(D2207-Pad2) -> Net-(D2103-Pad3)
- R2232 pad 2: Net-(D2208-Pad2) -> Net-(D2104-Pad3)
- R2233 pad 1: Net-(D2303-Pad2) -> Net-(D2204-Pad3)
- R2234 pad 1: Net-(D2305-Pad2) -> Net-(D2207-Pad3)
- R2235 pad 1: Net-(D2307-Pad2) -> Net-(D2208-Pad3)
- R2301 pad 1: (no net) -> /Analog inputs/10V-1-4/A_in
- R2301 pad 2: Net-(D2301-Pad2) -> Net-(D2203-Pad3)
- R2302 pad 1: Net-(D2301-Pad2) -> Net-(D2203-Pad3)
- R2303 pad 1: (no net) -> /Analog inputs/10V-1-4/B_in
- R2303 pad 2: Net-(D2303-Pad2) -> Net-(D2204-Pad3)
- R2305 pad 1: (no net) -> /Analog inputs/10V-1-4/C_in
- R2305 pad 2: Net-(D2305-Pad2) -> Net-(D2207-Pad3)
- R2307 pad 1: (no net) -> /Analog inputs/10V-1-4/D_in
- R2307 pad 2: Net-(D2307-Pad2) -> Net-(D2208-Pad3)
- R2309 pad 2: Net-(D2301-Pad2) -> Net-(D2203-Pad3)
- R2310 pad 2: Net-(D2303-Pad2) -> Net-(D2204-Pad3)
- R2311 pad 2: Net-(D2305-Pad2) -> Net-(D2207-Pad3)
- R2312 pad 2: Net-(D2307-Pad2) -> Net-(D2208-Pad3)
- R2405 pad 1: Net-(D2401-Pad2) -> Net-(D2301-Pad3)
- R2406 pad 1: Net-(D2403-Pad2) -> Net-(D2302-Pad3)
- R2407 pad 1: Net-(D2405-Pad2) -> Net-(D2303-Pad3)
- R2408 pad 1: Net-(D2407-Pad2) -> Net-(D2304-Pad3)
- R2409 pad 2: Net-(D2401-Pad2) -> Net-(D2301-Pad3)
- R2410 pad 2: Net-(D2403-Pad2) -> Net-(D2302-Pad3)
- R2411 pad 2: Net-(D2405-Pad2) -> Net-(D2303-Pad3)
- R2412 pad 2: Net-(D2407-Pad2) -> Net-(D2304-Pad3)
- R701 pad 2: Net-(D701-Pad2) -> Net-(D701-Pad1)
- U201 pad 2: (no net) -> Net-(U201-Pad2)
- U201 pad 3: (no net) -> Net-(U201-Pad3)
- U301 pad 5: (no net) -> Net-(U301-Pad5)
- U302 pad 5: (no net) -> Net-(U302-Pad5)
- U601 pad 10: (no net) -> Net-(U601-Pad10)
- U601 pad 15: (no net) -> Net-(U601-Pad15)
- U601 pad 16: (no net) -> Net-(U601-Pad16)
- U601 pad 7: (no net) -> Net-(U601-Pad7)
